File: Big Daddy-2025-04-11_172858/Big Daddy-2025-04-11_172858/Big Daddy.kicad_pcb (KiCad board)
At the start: 4 copper layers, 245.7 x 126.7 mm, 127 parts, among them J1 BMS Button, J10 Conn_01x02, J11 Conn_01x23, J12 Conn_01x14, J13 Conn_01x14, J15 Conn_01x02, J2 IMD Button, J3 HV+, J4 HV-, J5 GND, J6 HV+, J7 HV-, J8 Conn_01x14, J9 Conn_01x08, K1 T9VV1K15-12S, K2 G5V-2, K3 G5V-2, K4 J107, K5 G5V-1, Q1 2N7002, Q2 BCP53, Q3 IXFH34N65X2, Q4 IXFH34N65X2, Q6 MMBT2222, U1 MAX33054EASA+T, U10 TLP184, U11 LM5050-1, U12 LM5050-1, U14 LM317_TO-263, U2 ESP32-S3-DevKitC, U3 ESP32-S3-DevKitC, U4 LT1528CQ#PBF, U5 LTV-817S, U6 ICM7555xB, U7 IS31LT3360, U8 Vicor_AERO, U9 LTV-817S

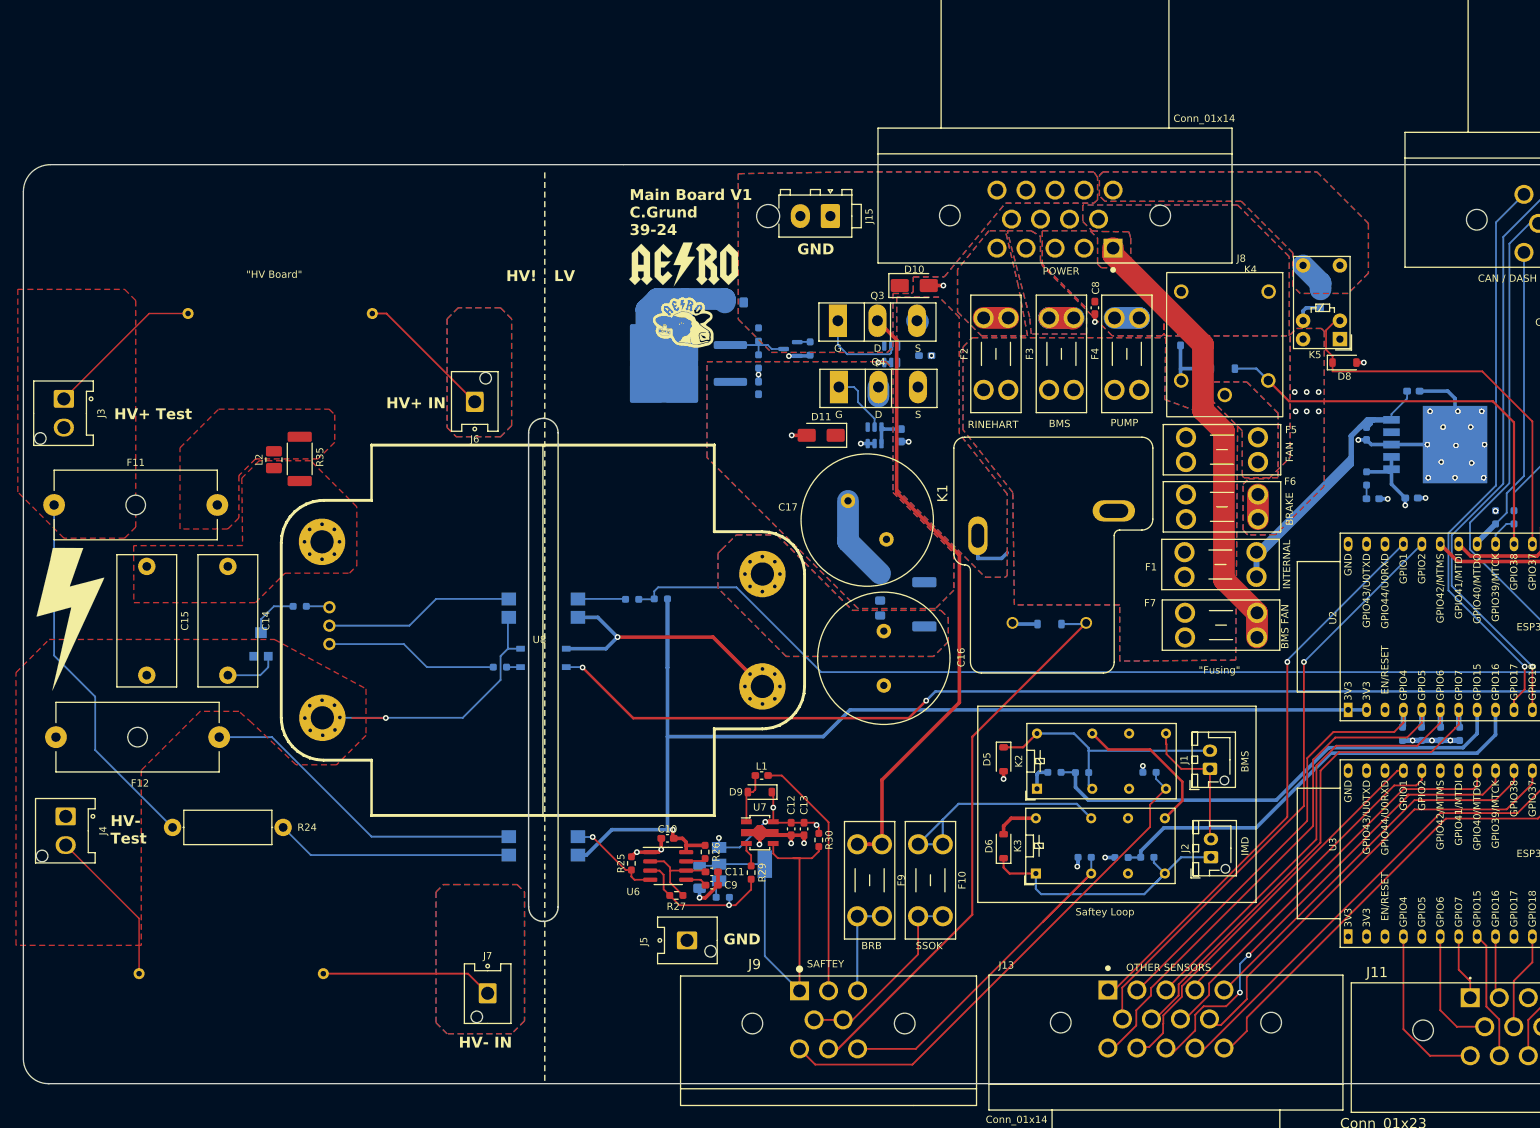
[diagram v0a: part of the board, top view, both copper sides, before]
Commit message: PCB fixes
BMS relay
C12 footprint
TSMP resistor connections
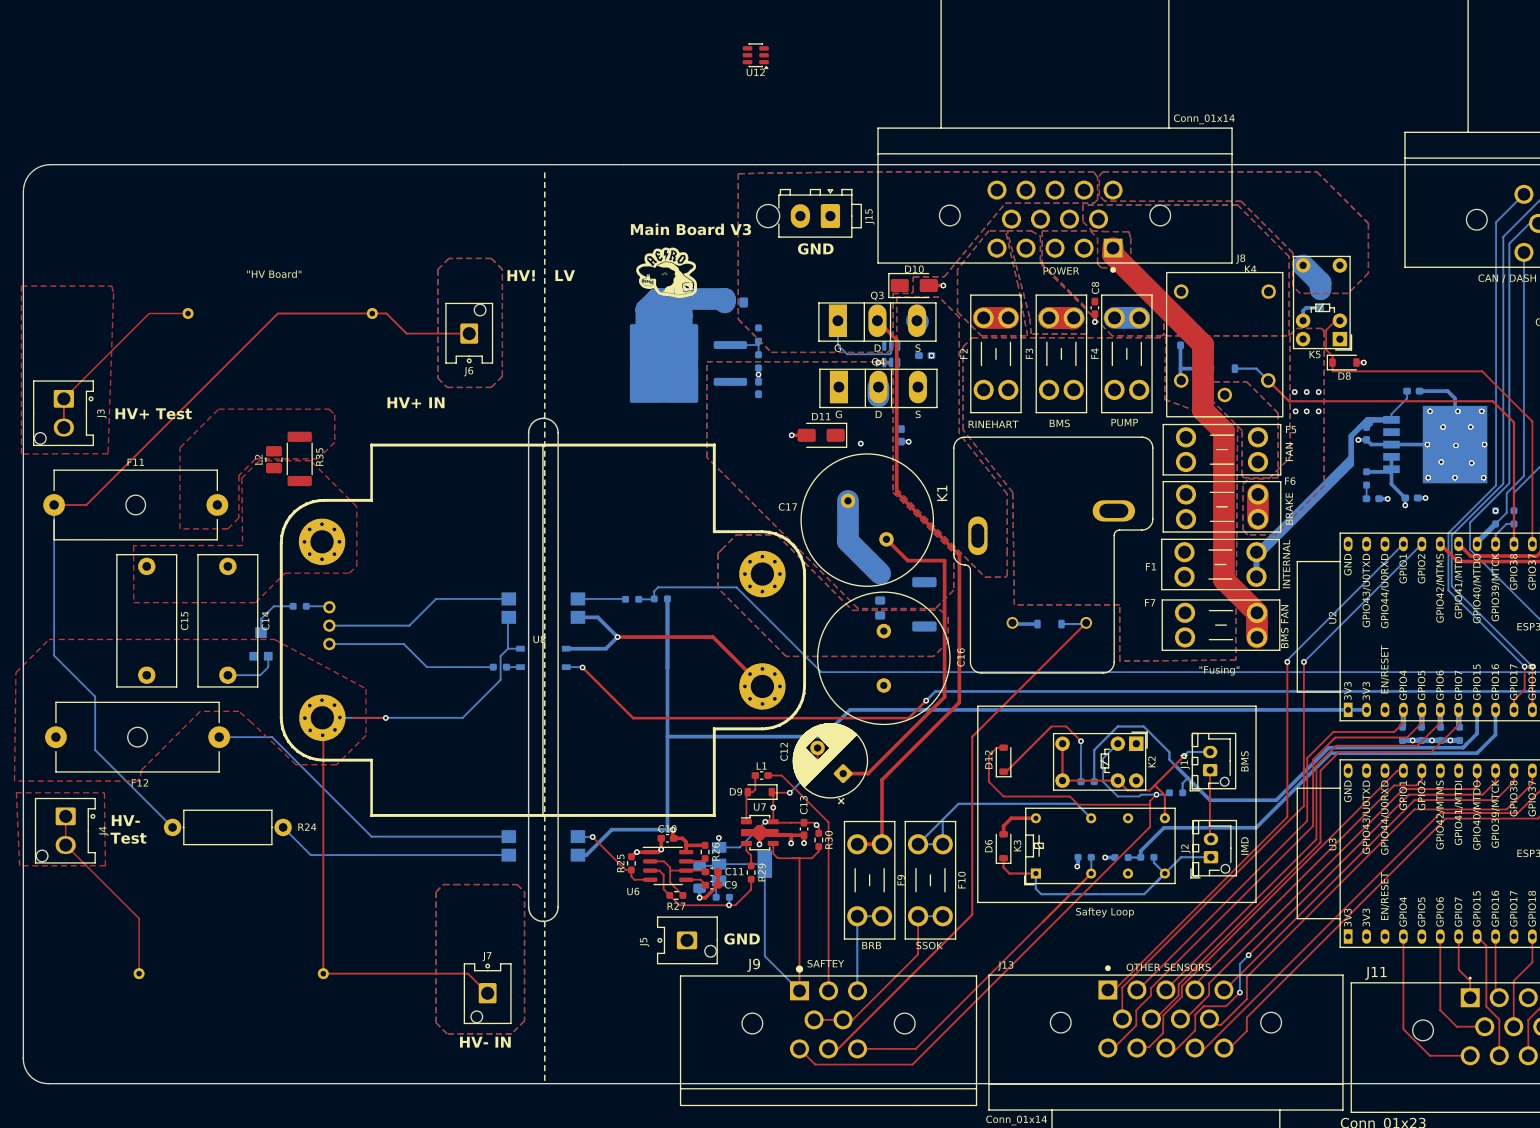
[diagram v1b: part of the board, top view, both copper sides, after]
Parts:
- removed D5: 1N4148W, Diode_SMD:D_SOD-123
- removed the G*** at (69.5, 123.5)
- removed the G*** at (154.0, 74.5)
- removed J1: BMS Button, Connector_JST:JST_XH_B2B-XH-AM_1x02_P2.50mm_Vertical
- removed Q6: MMBT2222, Package_TO_SOT_SMD:SOT-23
- removed R18: 10k, Resistor_SMD:R_0603_1608Metric_Pad0.98x0.95mm_HandSolder
- removed R19: 5.97k, Resistor_SMD:R_0603_1608Metric_Pad0.98x0.95mm_HandSolder
- removed R20: 2.2k, Resistor_SMD:R_0603_1608Metric_Pad0.98x0.95mm_HandSolder
- added D12: 1N4148W, Diode_SMD:D_SOD-123, F.Cu at (198.1, 142.7)
- added J14: BMS Button, Connector_JST:JST_XH_B2B-XH-AM_1x02_P2.50mm_Vertical, F.Cu at (226.6, 144.2)
- added R16: 5.97k, Resistor_SMD:R_0603_1608Metric_Pad0.98x0.95mm_HandSolder, B.Cu at (209.7, 145.8)
- C12: footprint Capacitor_SMD:C_0603_1608Metric_Pad1.08x0.95mm_HandSolder -> Capacitor_THT:CP_Radial_D10.0mm_P5.00mm
- K2: value G5V-2 -> G5V-1; footprint Relay_THT:Relay_DPDT_Omron_G5V-2 -> Relay_THT:Relay_SPDT_Omron_G5V-1
- R41: value 100 -> 2.2k
- U12: moved to F.Cu
- moved R41 79.3 mm to (221.9, 147.3), turned to 180 degrees
- moved U12 54.9 mm to (164.0, 45.7), turned to 180 degrees
- moved K2 15.0 mm to (216.4, 140.6), turned to -90 degrees
- moved C12 10.5 mm to (176.0, 144.7), turned to 135 degrees
- moved J6 9.43 mm to (124.5, 84.0)
- moved G*** 7.24 mm to (151.7, 76.1)
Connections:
- J3 pad 1: /High Voltage/TSAL/HV+ -> Net-(J3-Pin_1)
- J3 pad 2: /High Voltage/TSAL/HV+ -> Net-(J3-Pin_1)
- J4 pad 1: /High Voltage/DCDC/HV- -> Net-(J4-Pin_1)
- J4 pad 2: /High Voltage/DCDC/HV- -> Net-(J4-Pin_1)
- J6 pad 1: Net-(J6-Pin_1) -> /High Voltage/TSAL/HV+
- J7 pad 1: Net-(J7-Pin_1) -> /High Voltage/DCDC/HV-
- K2 pad 1: GND -> unconnected-(K2-Pad1)
- K2 pad 6: unconnected-(K2-Pad6) -> /Latching/BMS_Switch
- K2 pad 9: INT_12V -> /Latching/BMS_Switch
- K3 pad 9: Net-(K2-Pad13) -> /Latching/BMS_Switch
- R32 pad 1: /High Voltage/TSAL/HV+ -> Net-(J3-Pin_1)
- R32 pad 2: Net-(J6-Pin_1) -> /High Voltage/TSAL/HV+
- R33 pad 1: /High Voltage/DCDC/HV- -> Net-(J4-Pin_1)
- R33 pad 2: Net-(J7-Pin_1) -> /High Voltage/DCDC/HV-
- R41 pad 1: Net-(Q6-B) -> /Latching/BMS_IND
- R41 pad 2: GND -> /Connectors/BMS_FAULT_SIG
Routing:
- net /High Voltage/TSAL/HV+: track 73.2 -> 121.6 mm
- net /Connectors/BMS_FAULT_SIG: track 72.2 -> 113.5 mm, vias 0 -> 1
- net /High Voltage/DCDC/HV-: track 71.5 -> 108.7 mm
- net GND: track 162.2 -> 198.3 mm, vias 49 -> 46
- net Net-(J3-Pin_1): track 0.00 -> 26.0 mm
- net Net-(J4-Pin_1): track 0.00 -> 25.9 mm
- net Net-(J7-Pin_1): track 23.8 -> 0.00 mm
- net Net-(K2-Pad13): track 21.2 -> 0.00 mm
- net Net-(D12-K): track 0.00 -> 19.8 mm, vias 0 -> 1
- net Net-(J6-Pin_1): track 19.2 -> 0.00 mm
- net /Fusing/12_prefuse: track 12.8 -> 0.20 mm
- net Net-(Q6-C): track 9.44 -> 0.00 mm
- net Net-(Q4-G): track 8.77 -> 0.00 mm
- net Net-(U14-ADJ): track 0.00 -> 5.76 mm
- net /Latching/BMS_IND: track 67.2 -> 72.7 mm
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- added copper zone on B.Cu, net /High Voltage/DCDC/HV-
- added copper zone on B.Cu, net /High Voltage/TSAL/HV+
- removed copper zone on B.Cu, net Net-(J6-Pin_1)
- removed copper zone on F.Cu, net Net-(J6-Pin_1)
- removed copper zone on B.Cu, net Net-(J7-Pin_1)
- removed copper zone on F.Cu, net Net-(J7-Pin_1)
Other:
- outline, holes or cut-outs redrawn
- board text added: "Main Board V3"
- board text removed: "Main Board V1 C.Grund 39-24"

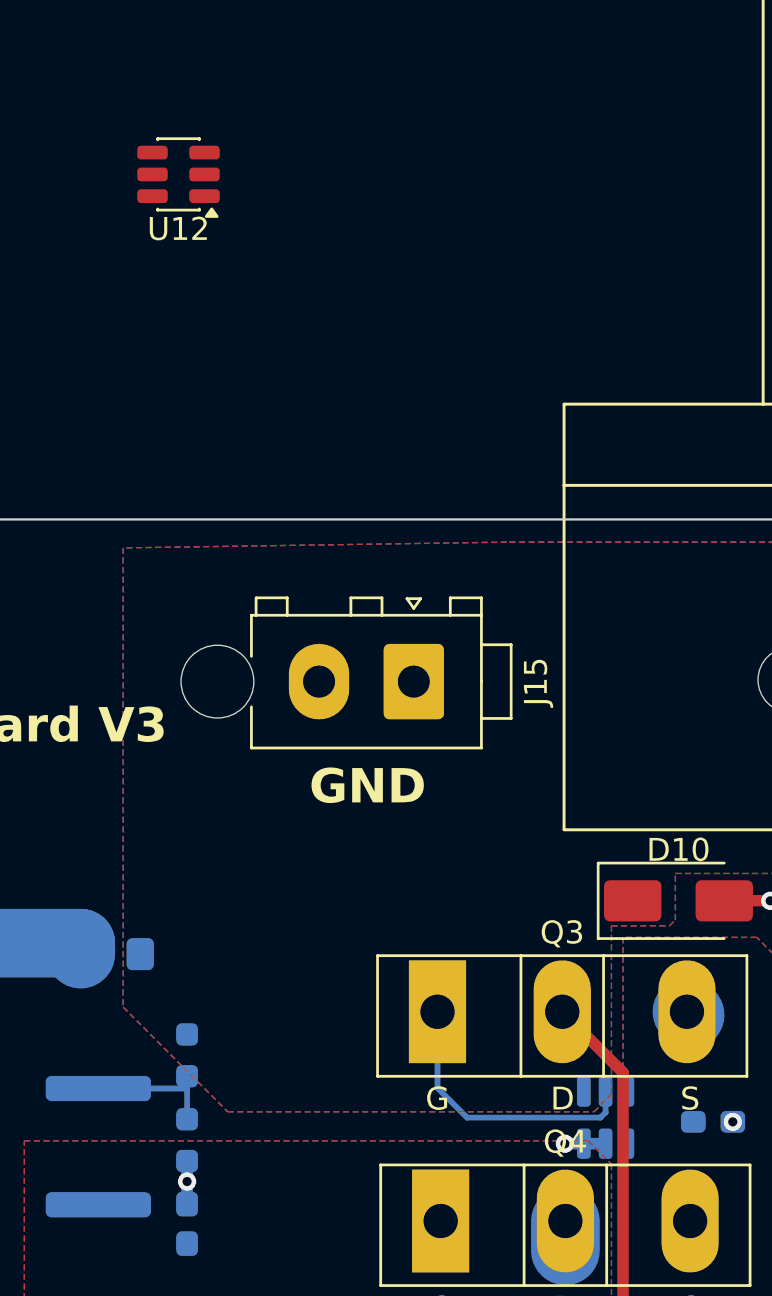
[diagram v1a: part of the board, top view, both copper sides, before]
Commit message: BMS Indicator
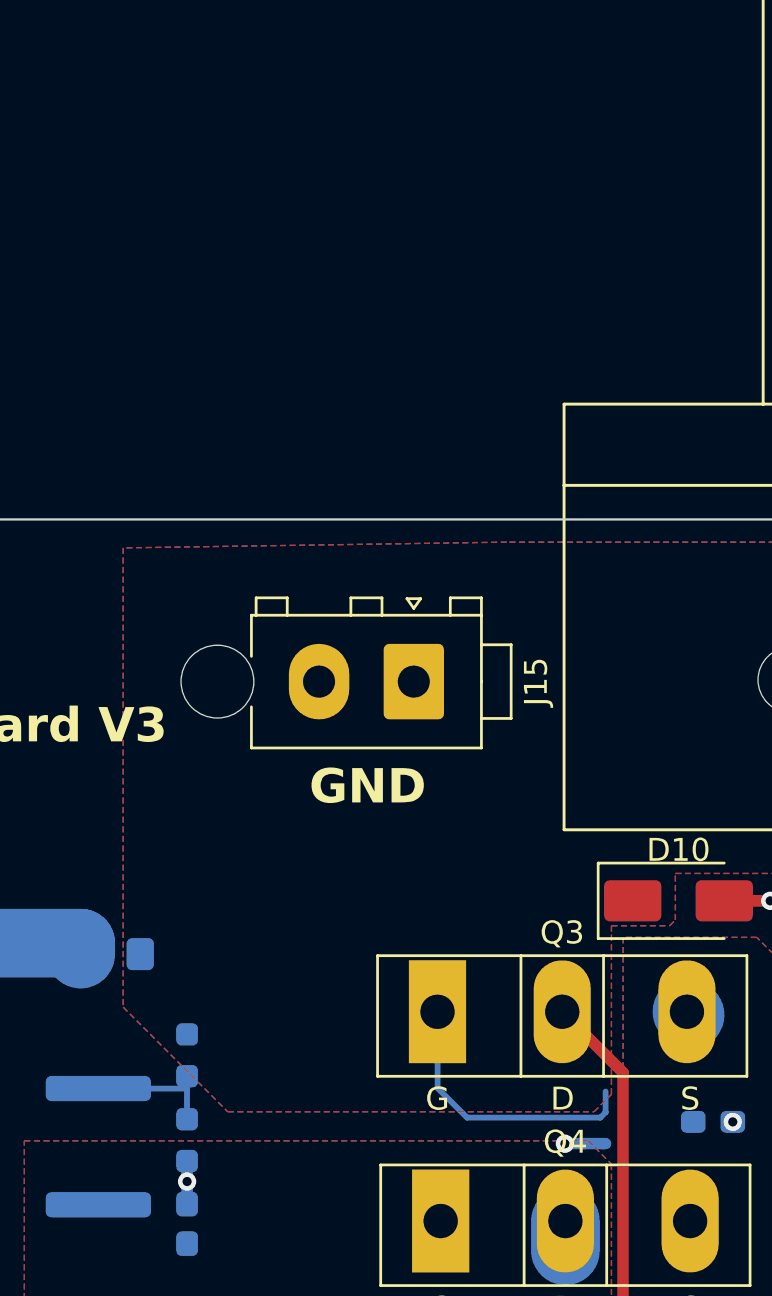
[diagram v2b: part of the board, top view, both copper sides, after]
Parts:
- removed U11, U12: LM5050-1, Package_TO_SOT_SMD:TSOT-23-6
